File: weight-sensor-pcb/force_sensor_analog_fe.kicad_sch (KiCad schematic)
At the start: 10 parts, among them U2 INA333xxDRG

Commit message: test
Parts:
- removed C1, C2, C3, C4: 0.1u, symbol Device:C
- removed R1: 4k, symbol Device:R
- removed R2, R3: 10k, symbol Device:R
- removed R4: 1k, symbol Device:R
- removed U1: ~, symbol force_sensor_symbols:HSFPAR007A
- removed U2: INA333xxDRG, Package_SON:WSON-8-1EP_3x3mm_P0.5mm_EP1.45x2.4mm, symbol Amplifier_Instrumentation:INA333xxDRG

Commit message: Transfered LTSpice analog schematic to its appropriate schematic page
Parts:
- added IC2: HSFPAR004A, HSFPAR004A, symbol Capstone:HSFPAR004A
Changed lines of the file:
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@@
 		(title "Force Sensor & Analog Front-End")
 	)
+	(symbol
+		(lib_id "Capstone:HSFPAR004A")
+		(at 48.26 83.82 0)
+		(unit 1)
+		(exclude_from_sim no)
+		(in_bom yes)
+		(on_board yes)
+		(dnp no)
+		(fields_autoplaced yes)
+		(property "Reference" "IC2"
+			(at 63.5 76.2 0)
+			(effects
+				(font
+					(size 1.27 1.27)
+				)
+			)
+		)
+		(property "Value" "HSFPAR004A"
+			(at 63.5 78.74 0)
+			(effects
+				(font
+					(size 1.27 1.27)
+				)
+			)
+		)
+		(property "Footprint" "HSFPAR004A"
+			(at 74.93 178.74 0)
+			(effects
+				(font
+					(size 1.27 1.27)
+				)
+				(justify left top)
+				(hide yes)
+			)
+		)
+		(property "Datasheet" "https://eu.mouser.com/datasheet/2/15/Alps_09242019_HSFPAR004A_datasheet-1651683.pdf"
+			(at 74.93 278.74 0)
+			(effects
+				(font
+					(size 1.27 1.27)
+				)
+				(justify left top)
+				(hide yes)
+			)
+		)
+		(property "Description" "Resistive Force Sensor 0.82kgf (1.8lbs)"
+			(at 48.26 83.82 0)
+			(effects
+				(font
+					(size 1.27 1.27)
+				)
+				(hide yes)
+			)
+		)
+		(property "Height" "0.66"
+			(at 74.93 478.74 0)
+			(effects
+				(font
+					(size 1.27 1.27)
+				)
+				(justify left top)
+				(hide yes)
+			)
+		)
+		(property "Manufacturer_Name" "ALPS Electric"
+			(at 74.93 578.74 0)
+			(effects
+				(font
+					(size 1.27 1.27)
+				)
+				(justify left top)
+				(hide yes)
+			)
+		)
+		(property "Manufacturer_Part_Number" "HSFPAR004A"
+			(at 74.93 678.74 0)
+			(effects
+				(font
+					(size 1.27 1.27)
+				)
+				(justify left top)
+				(hide yes)
+			)
+		)
+		(property "Mouser Part Number" "688-HSFPAR004A"
+			(at 74.93 778.74 0)
+			(effects
+				(font
+					(size 1.27 1.27)
+				)
+				(justify left top)
+				(hide yes)
+			)
+		)
+		(property "Mouser Price/Stock" "https://www.mouser.co.uk/ProductDetail/Alps-Alpine/HSFPAR004A?qs=XeJtXLiO41SKORml6bvmQg%3D%3D"
+			(at 74.93 878.74 0)
+			(effects
+				(font
+					(size 1.27 1.27)
+				)
+				(justify left top)
+				(hide yes)
+			)
+		)
+		(property "Arrow Part Number" ""
+			(at 74.93 978.74 0)
+			(effects
+				(font
+					(size 1.27 1.27)
+				)
+				(justify left top)
+				(hide yes)
+			)
+		)
+		(property "Arrow Price/Stock" ""
+			(at 74.93 1078.74 0)
+			(effects
+				(font
+					(size 1.27 1.27)
+				)
+				(justify left top)
+				(hide yes)
+			)
+		)
+		(pin "2"
+		)
+		(pin "5"
+		)
+		(pin "4"
+		)
+		(pin "1"
+		)
+		(pin "3"
+		)
+		(instances
+			(project ""
+				(path "/030ca1f5-68f0-4323-9a91-656d7965b13e/6677df09-7d73-4890-91f9-2c1f8721421d"
+					(reference "IC2")
+					(unit 1)
+				)
+			)
+		)
+	)
 )

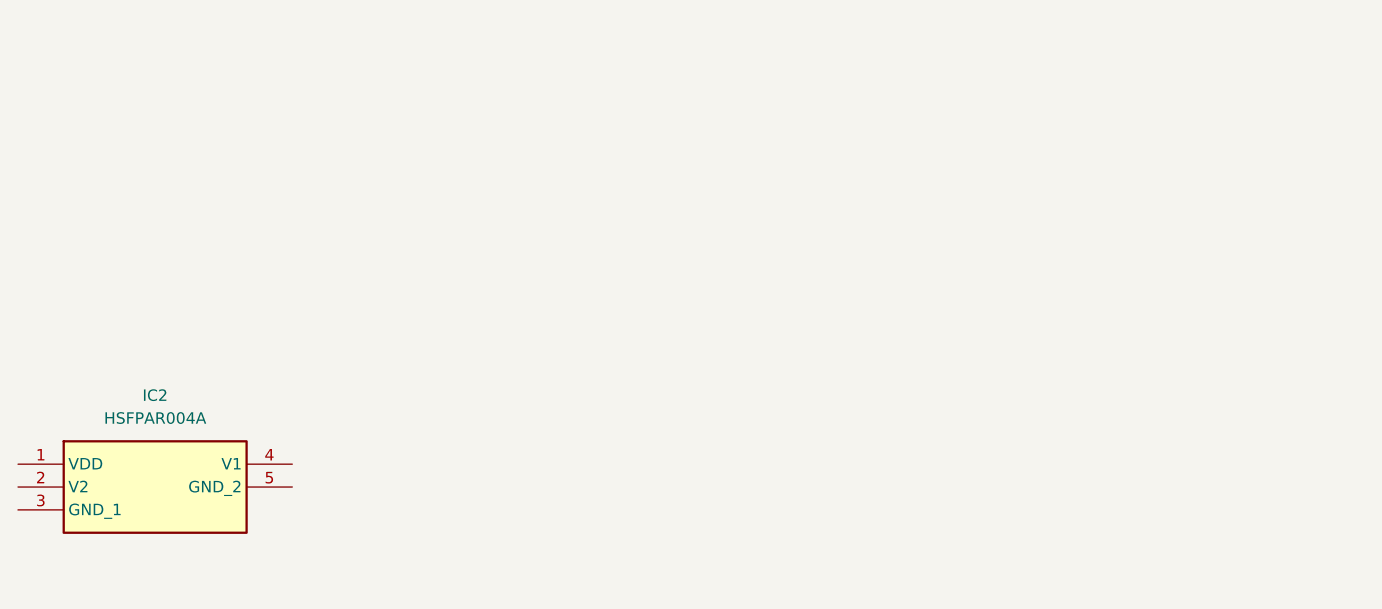
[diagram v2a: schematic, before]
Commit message: schematic clean up
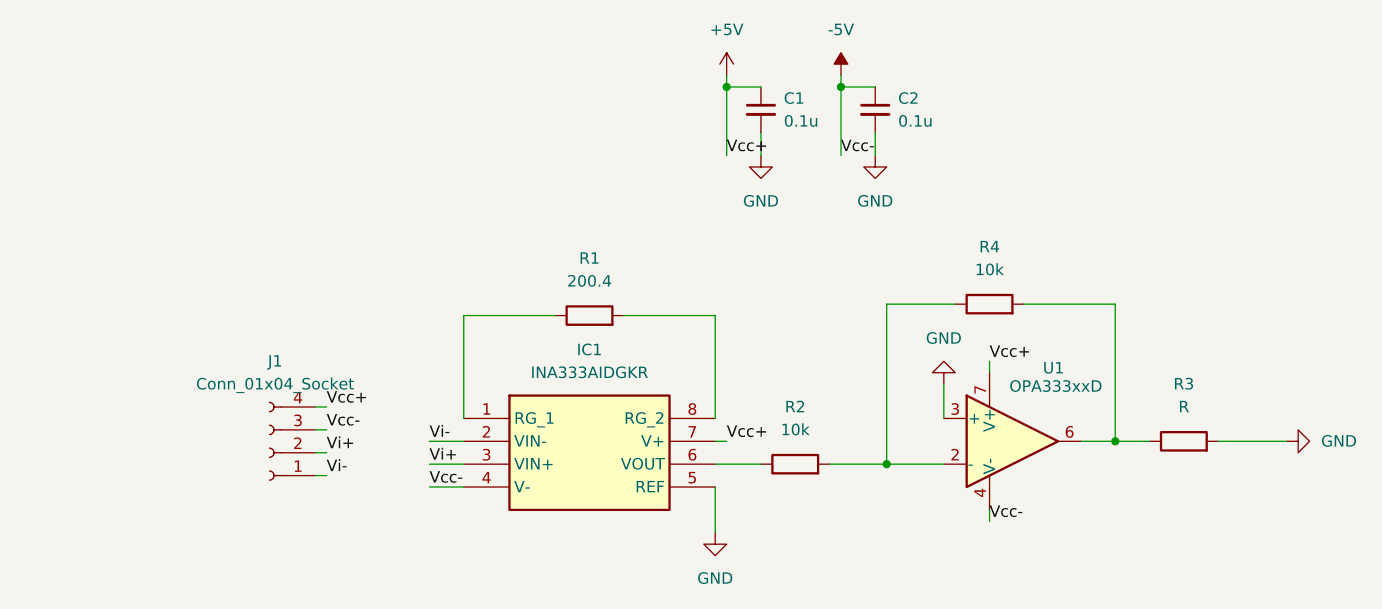
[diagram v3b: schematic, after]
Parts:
- removed IC2: HSFPAR004A, HSFPAR004A, symbol Capstone:HSFPAR004A
- added C1, C2: 0.1u, symbol Device:C_Small
- added IC1: INA333AIDGKR, SOP65P490X110-8N, symbol Capstone:INA333AIDGKR
- added J1: Conn_01x04_Socket, symbol Connector:Conn_01x04_Socket
- added R1: 200.4, symbol Device:R
- added R2, R4: 10k, symbol Device:R
- added R3: R, symbol Device:R
- added U1: OPA333xxD, Package_SO:SOIC-8_3.9x4.9mm_P1.27mm, symbol Amplifier_Operational:OPA333xxD
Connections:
- new net: R2.2, R4.1, U1.2 (-)
- new net: R3.1, R4.2, U1.6
- new net: IC1.6 (VOUT), R2.1
- new net: IC1.1 (RG_1), R1.1
- new net: IC1.8 (RG_2), R1.2
- new net +5V: C1.1, IC1.7 (V+), J1.4 (Pin_4), U1.7 (V+)
- new net -5V: C2.1, IC1.4 (V-), J1.3 (Pin_3), U1.4 (V-)
- new net GND: C1.2, C2.2, IC1.5 (REF), R3.2, U1.3 (+)
- new net Vi+: IC1.3 (VIN+), J1.2 (Pin_2)
- new net Vi-: IC1.2 (VIN-), J1.1 (Pin_1)

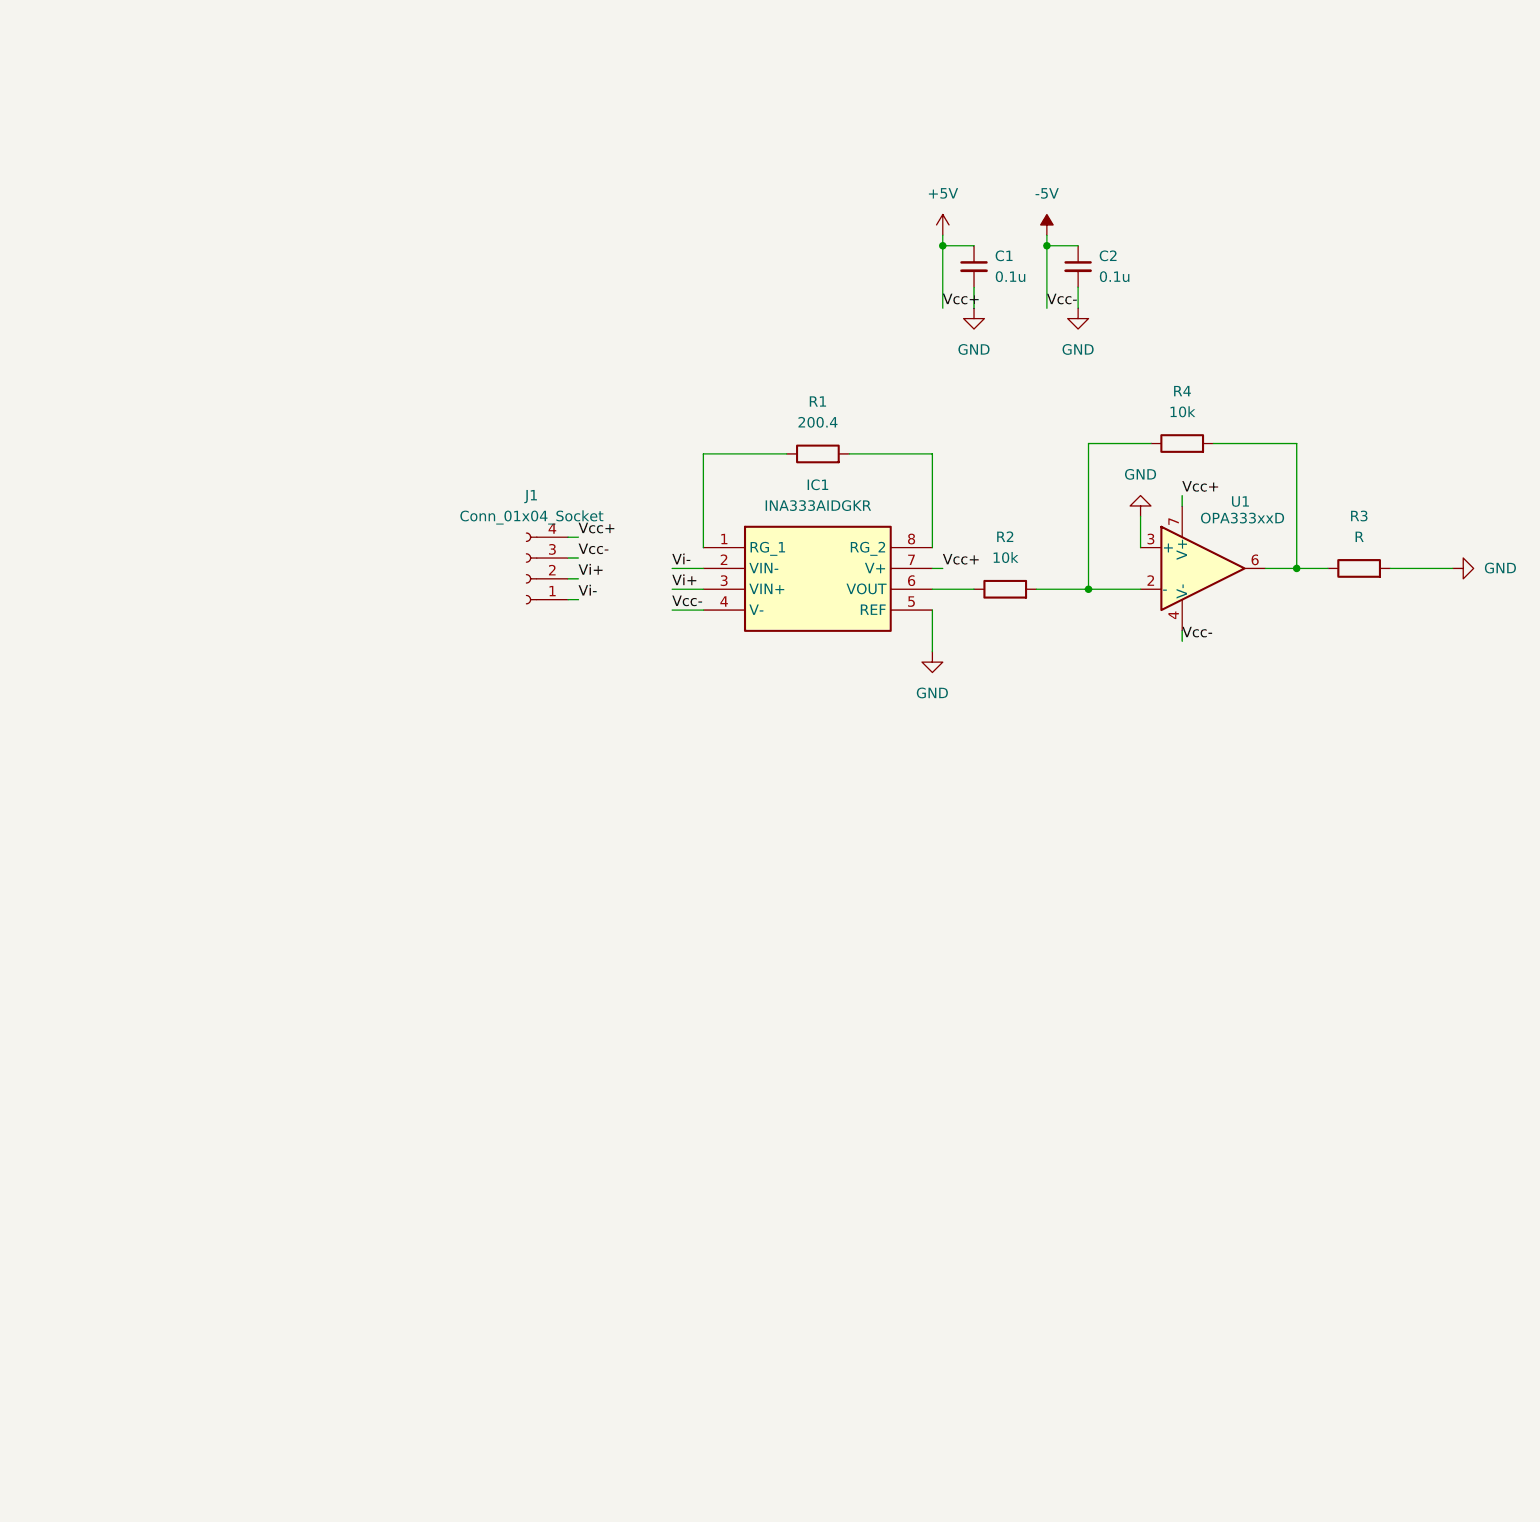
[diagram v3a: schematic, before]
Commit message: further schematic clean up
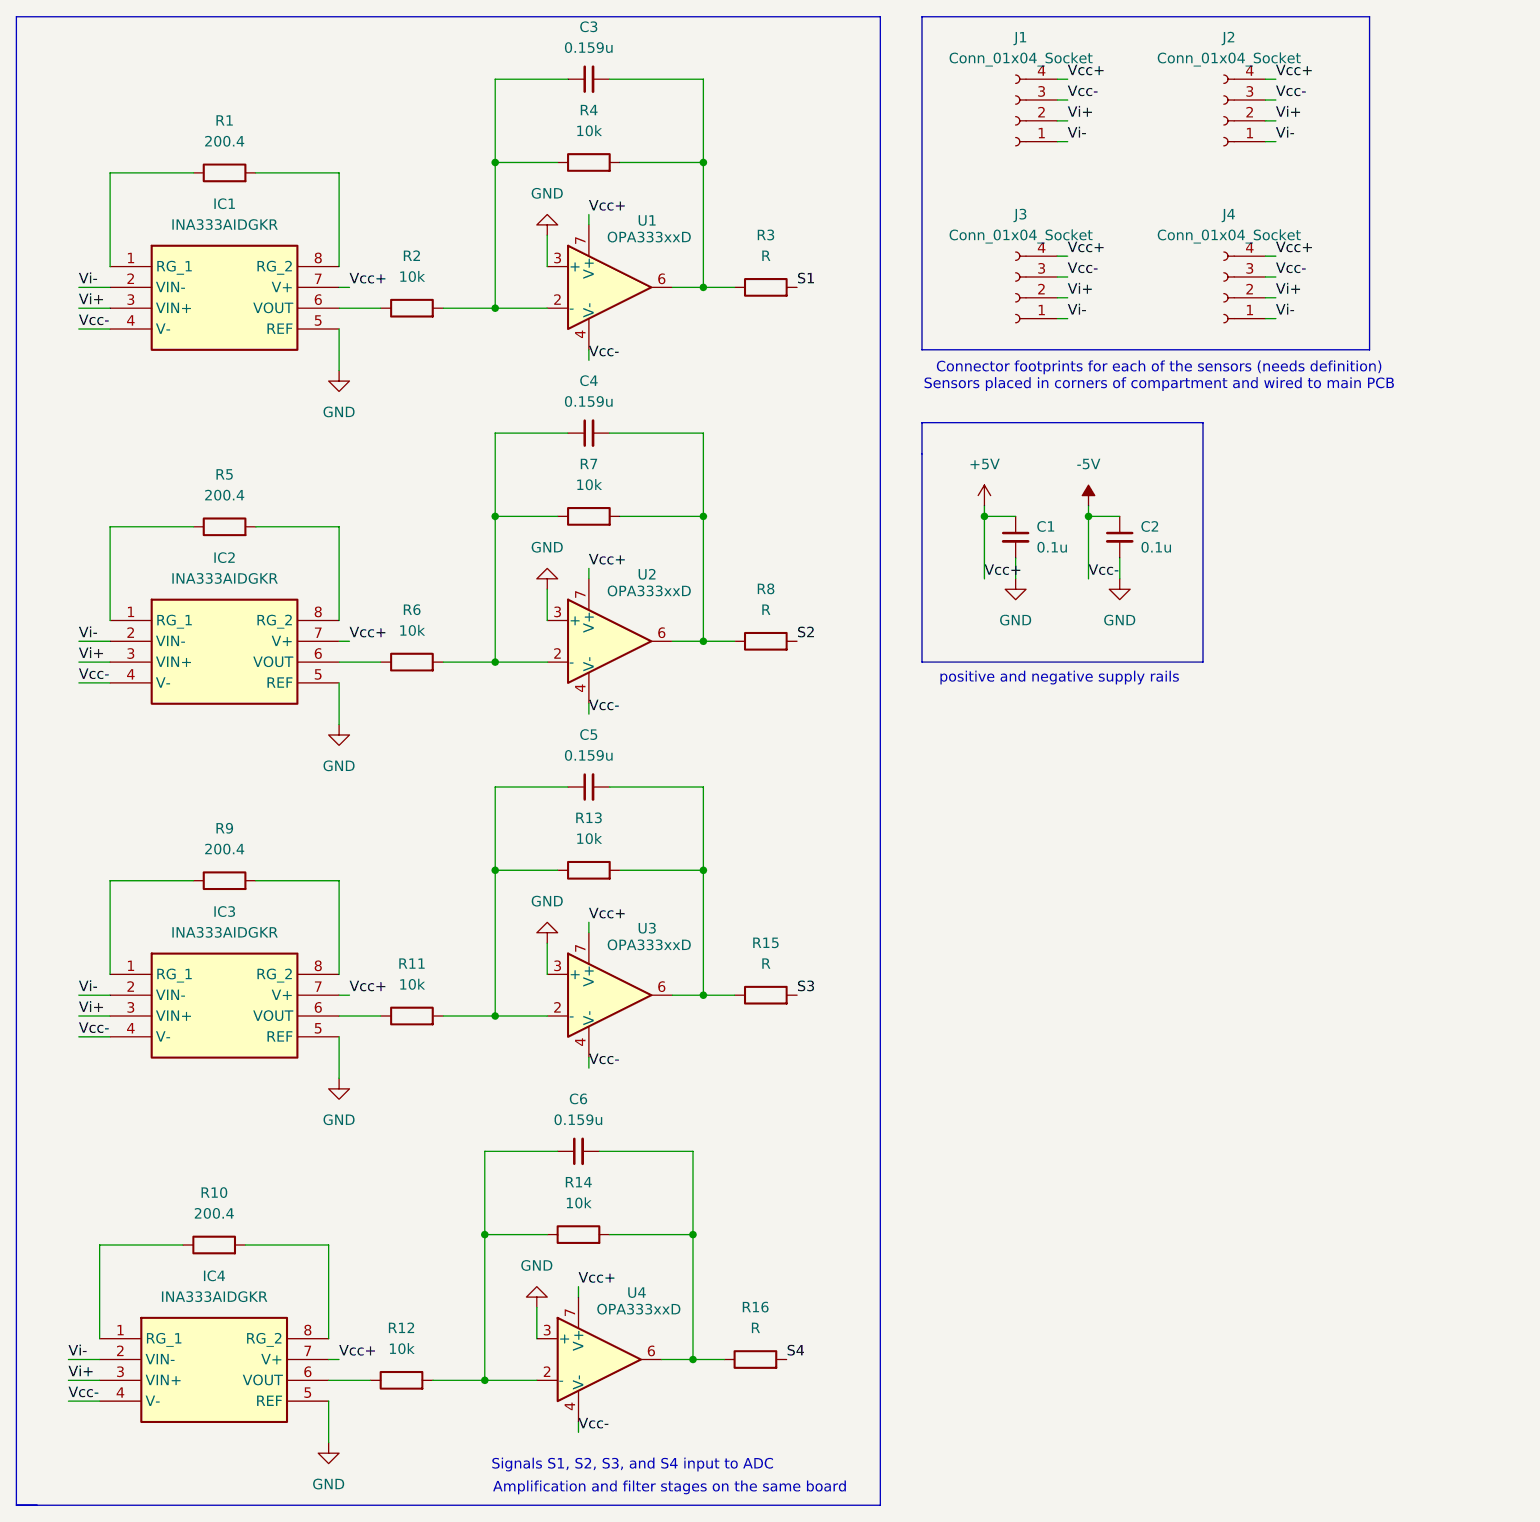
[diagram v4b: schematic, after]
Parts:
- added C3, C4, C5, C6: 0.159u, symbol Device:C_Small
- added IC2, IC3, IC4: INA333AIDGKR, SOP65P490X110-8N, symbol Capstone:INA333AIDGKR
- added J2, J3, J4: Conn_01x04_Socket, symbol Connector:Conn_01x04_Socket
- added R10, R5, R9: 200.4, symbol Device:R
- added R11, R12, R13, R14, R6, R7: 10k, symbol Device:R
- added R15, R16, R8: R, symbol Device:R
- added U2, U3, U4: OPA333xxD, Package_SO:SOIC-8_3.9x4.9mm_P1.27mm, symbol Amplifier_Operational:OPA333xxD
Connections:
- net +5V: now also IC2.7 (V+), IC3.7 (V+), IC4.7 (V+), J2.4 (Pin_4), J3.4 (Pin_4), J4.4 (Pin_4), U2.7 (V+), U3.7 (V+), U4.7 (V+)
- net -5V: now also IC2.4 (V-), IC3.4 (V-), IC4.4 (V-), J2.3 (Pin_3), J3.3 (Pin_3), J4.3 (Pin_3), U2.4 (V-), U3.4 (V-), U4.4 (V-)
- net GND: now also IC2.5 (REF), IC3.5 (REF), IC4.5 (REF), U2.3 (+), U3.3 (+), U4.3 (+); no longer R3.2
- net Vi+: now also IC2.3 (VIN+), IC3.3 (VIN+), IC4.3 (VIN+), J2.2 (Pin_2), J3.2 (Pin_2), J4.2 (Pin_2)
- net Vi-: now also IC2.2 (VIN-), IC3.2 (VIN-), IC4.2 (VIN-), J2.1 (Pin_1), J3.1 (Pin_1), J4.1 (Pin_1)
- net at R2.2, R4.1, U1.2 (-): now also C3.1
- net at R3.1, R4.2, U1.6: now also C3.2
- new net: C4.1, R6.2, R7.1, U2.2 (-)
- new net: C4.2, R7.2, R8.1, U2.6
- new net: IC4.6 (VOUT), R12.1
- new net: C6.1, R12.2, R14.1, U4.2 (-)
- new net: IC4.1 (RG_1), R10.1
- new net: IC4.8 (RG_2), R10.2
- new net: IC2.6 (VOUT), R6.1
- new net: C5.2, R13.2, R15.1, U3.6
- new net: C6.2, R14.2, R16.1, U4.6
- new net: IC3.1 (RG_1), R9.1
- new net: IC3.6 (VOUT), R11.1
- new net: IC3.8 (RG_2), R9.2
- new net: IC2.1 (RG_1), R5.1
- new net: IC2.8 (RG_2), R5.2
- new net: C5.1, R11.2, R13.1, U3.2 (-)
- new net S1: R3.2
- new net S2: R8.2
- new net S3: R15.2
- new net S4: R16.2
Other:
- note added: "Amplification and filter stages on the same board"
- note added: "Connector footprints for each of the sensors (needs definition) Sensors placed in corners of compartment and wired to main PCB"
- note added: "Signals S1, S2, S3, and S4 input to ADC"
- note added: "positive and negative supply rails"
- moved on the sheet: C1, C2, IC1, J1, R1, R2, R3, R4, U1
